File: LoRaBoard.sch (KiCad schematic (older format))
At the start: 22 parts, among them J1 Prog, J2 I2C, J3 UART, J4 GPIO, J5 ADC/SPI, J6 CONN_01X02, J7 PWR, SW1 SWITCH_PUSHBUTTONC&K_KSS, U1 im880b, U2 LDO-TPS78233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

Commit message: Done, panelize
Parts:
- added J8: CONN_01X01, Pin_Headers:Pin_Header_Straight_1x01_Pitch2.54mm, symbol CONN_01X01
- gave numbers to parts that had none: 2
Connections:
- net +3V3: now also J8.1 (P1)
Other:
- moved on the sheet: J7
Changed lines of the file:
@@
 L CONN_01X02 J7
 U 1 1 58D21A9B
-P 9500 750
-F 0 "J7" H 9500 900 50  0000 C CNN
-F 1 "PWR" V 9600 750 50  0000 C CNN
-F 2 "Pin_Headers:Pin_Header_Straight_1x02_Pitch2.54mm" H 9500 750 50  0001 C CNN
-F 3 "" H 9500 750 50  0001 C CNN
-	1    9500 750
+P 9300 750
+F 0 "J7" H 9300 900 50  0000 C CNN
+F 1 "PWR" V 9400 750 50  0000 C CNN
+F 2 "Pin_Headers:Pin_Header_Straight_1x02_Pitch2.54mm" H 9300 750 50  0001 C CNN
+F 3 "" H 9300 750 50  0001 C CNN
+	1    9300 750
 	0    -1   -1   0
 $EndComp
@@
 L GND #PWR01
 U 1 1 58D237F2
-P 9600 950
-F 0 "#PWR01" H 9600 700 50  0001 C CNN
-F 1 "GND" H 9600 800 50  0000 C CNN
-F 2 "" H 9600 950 50  0001 C CNN
-F 3 "" H 9600 950 50  0001 C CNN
-	1    9600 950
+P 9400 950
+F 0 "#PWR01" H 9400 700 50  0001 C CNN
+F 1 "GND" H 9400 800 50  0000 C CNN
+F 2 "" H 9400 950 50  0001 C CNN
+F 3 "" H 9400 950 50  0001 C CNN
+	1    9400 950
 	1    0    0    -1
 $EndComp
@@
 L +BATT #PWR014
 U 1 1 58D245EB
-P 9400 950
-F 0 "#PWR014" H 9400 800 50  0001 C CNN
-F 1 "+BATT" H 9400 1090 50  0000 C CNN
-F 2 "" H 9400 950 50  0001 C CNN
-F 3 "" H 9400 950 50  0001 C CNN
-	1    9400 950
+P 9200 950
+F 0 "#PWR014" H 9200 800 50  0001 C CNN
+F 1 "+BATT" H 9200 1090 50  0000 C CNN
+F 2 "" H 9200 950 50  0001 C CNN
+F 3 "" H 9200 950 50  0001 C CNN
+	1    9200 950
 	-1   0    0    1
 $EndComp
@@
 $EndComp
 Wire Wire Line
-	9450 950  9400 950
-Wire Wire Line
-	9550 950  9600 950
+	9250 950  9200 950
+Wire Wire Line
+	9350 950  9400 950
 Wire Wire Line
 	9350 1600 9350 1650
@@
 	10350 6000 10350 6100
 $Comp
-L RESISTOR0603-RES R?
+L RESISTOR0603-RES R5
 U 1 1 58E2215E
 P 10750 900
-F 0 "R?" H 10600 959 50  0000 L BNN
+F 0 "R5" H 10600 959 50  0000 L BNN
 F 1 "10k" H 10600 770 50  0000 L BNN
 F 2 "Resistors_SMD:R_0603" H 10780 1050 20  0001 C CNN
@@
 $EndComp
 $Comp
-L RESISTOR0603-RES R?
+L RESISTOR0603-RES R4
 U 1 1 58E22264
 P 10450 650
-F 0 "R?" H 10300 709 50  0000 L BNN
+F 0 "R4" H 10300 709 50  0000 L BNN
 F 1 "33k" H 10300 520 50  0000 L BNN
 F 2 "Resistors_SMD:R_0603" H 10480 800 20  0001 C CNN
@@
 	10750 1100 10750 1150
 $Comp
-L GND #PWR?
+L GND #PWR032
 U 1 1 58E22571
 P 10750 1150
-F 0 "#PWR?" H 10750 900 50  0001 C CNN
+F 0 "#PWR032" H 10750 900 50  0001 C CNN
 F 1 "GND" H 10750 1000 50  0000 C CNN
 F 2 "" H 10750 1150 50  0001 C CNN
@@
 $EndComp
 $Comp
-L +BATT #PWR?
+L +BATT #PWR033
 U 1 1 58E225BE
 P 10200 650
-F 0 "#PWR?" H 10200 500 50  0001 C CNN
+F 0 "#PWR033" H 10200 500 50  0001 C CNN
 F 1 "+BATT" H 10200 790 50  0000 C CNN
 F 2 "" H 10200 650 50  0001 C CNN
@@
 Text Label 10900 650  0    60   ~ 0
 P17
+$Comp
+L +3.3V #PWR034
+U 1 1 58E338CA
+P 8650 950
+F 0 "#PWR034" H 8650 800 50  0001 C CNN
+F 1 "+3.3V" H 8650 1090 50  0000 C CNN
+F 2 "" H 8650 950 50  0001 C CNN
+F 3 "" H 8650 950 50  0001 C CNN
+	1    8650 950
+	-1   0    0    1
+$EndComp
+Wire Wire Line
+	8650 850  8650 950
+$Comp
+L CONN_01X01 J8
+U 1 1 58E343EA
+P 8650 650
+F 0 "J8" H 8650 750 50  0000 C CNN
+F 1 "CONN_01X01" V 8750 650 50  0000 C CNN
+F 2 "Pin_Headers:Pin_Header_Straight_1x01_Pitch2.54mm" H 8650 650 50  0001 C CNN
+F 3 "" H 8650 650 50  0001 C CNN
+	1    8650 650
+	0    -1   -1   0
+$EndComp
 $EndSCHEMATC

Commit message: Done
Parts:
- C2, C3: value 0.1u -> 1u
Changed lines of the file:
@@
 P 9950 5000
 F 0 "C3" H 9975 5100 50  0000 L CNN
-F 1 "0.1u" H 9975 4900 50  0000 L CNN
+F 1 "1u" H 9975 4900 50  0000 L CNN
 F 2 "Capacitors_SMD:C_0603" H 9988 4850 50  0001 C CNN
 F 3 "" H 9950 5000 50  0001 C CNN
@@
 P 9100 4600
 F 0 "C2" H 9125 4700 50  0000 L CNN
-F 1 "0.1u" H 8900 4700 50  0000 L CNN
+F 1 "1u" H 8900 4700 50  0000 L CNN
 F 2 "Capacitors_SMD:C_0603" H 9138 4450 50  0001 C CNN
 F 3 "" H 9100 4600 50  0001 C CNN

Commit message: PCB complete, panel complete
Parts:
- removed J1: Prog, Pin_Headers:Pin_Header_Straight_1x03_Pitch2.54mm, symbol CONN_01X03
- removed J2: I2C, Pin_Headers:Pin_Header_Straight_1x03_Pitch2.54mm, symbol CONN_01X03
- removed J3: UART, Pin_Headers:Pin_Header_Straight_1x03_Pitch2.54mm, symbol CONN_01X03
- removed J4: GPIO, Pin_Headers:Pin_Header_Straight_1x04_Pitch2.54mm, symbol CONN_01X04
- removed J5: ADC/SPI, Pin_Headers:Pin_Header_Straight_1x08_Pitch2.54mm, symbol CONN_01X08
- removed J6: CONN_01X02, Pin_Headers:Pin_Header_Straight_1x02_Pitch2.54mm, symbol CONN_01X02
- removed J8: CONN_01X01, Pin_Headers:Pin_Header_Straight_1x01_Pitch2.54mm, symbol CONN_01X01
- removed S1: SWITCH-SPDTPTH2, SparkFun-Electromechanical:SWITCH-SPDT-SMD, symbol SWITCH-SPDTPTH2
- removed SW1: SWITCH_PUSHBUTTONC&K_KSS, BTN_CK_KSS, symbol SWITCH_PUSHBUTTONC&K_KSS
- removed X1: SMACONNECTOR, adafruit:SMA90_DIP, symbol SMACONNECTOR
- added J1: CONN_01X12, Pin_Headers:Pin_Header_Straight_1x12_Pitch2.54mm, symbol CONN_01X12
- added J2: CONN_01X08, Pin_Headers:Pin_Header_Straight_1x08_Pitch2.54mm, symbol CONN_01X08
- added J3: CONN_01X09, Pin_Headers:Pin_Header_Straight_1x09_Pitch2.54mm, symbol CONN_01X09
- added J4: CONN_COAXIAL, Connectors:SMA_THT_Jack_Straight, symbol CONN_COAXIAL
- added J5: SwitchSPST, Buttons_Switches_SMD:SW_SPST_EVQPE1, symbol CONN_01X02
- added J6: CONN_01X01, Pin_Headers:Pin_Header_Straight_1x01_Pitch2.54mm, symbol CONN_01X01
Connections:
- net +3V3: now also J2.5 (P5), J5.1 (P1), J6.1 (P1)
- net +BATT: now also R1.2; no longer R1.1
- net GND: now also J1.11 (P11), J1.6 (P6), J2.4 (P4), J3.2 (P2), J3.7 (P7), J4.2 (Ext); no longer U1.1 (GND)
- net RF: now also J4.1 (In)
- net 4: now reaches U1.4 (P3/JTDO)
- net 4: now also J1.4 (P4)
- net 5: now reaches U1.5 (P4/JTDI)
- net 5: now also J1.5 (P5)
- net BOOT renamed 26
- net 26: now also J3.6 (P6)
- net EN: no longer names the net of U2.3 (EN)
- net EN: now also R1.1
- net JTCK renamed 2
- net 2: now also J1.2 (P2)
- net JTMS renamed 3
- net 3: now also J1.3 (P3)
- net P10 renamed 15
- net 15: now also J2.3 (P3)
- net P11 renamed 20
- net 20: now also J2.8 (P8)
- net P12 renamed 21
- net 21: now also J3.1 (P1)
- net P13 renamed 23
- net 23: now also J3.3 (P3)
- net P14 renamed 24
- net 24: now also J3.4 (P4)
- net P15 renamed 25
- net 25: now also J3.5 (P5)
- net P17 renamed 29
- net 29: now also J3.9 (P9)
- net P5 renamed 8
- net 8: now also J1.8 (P8)
- net P6 renamed 9
- net 9: now also J1.9 (P9)
- net P7 renamed 12
- net 12: now also J1.12 (P12)
- net P8 renamed 13
- net 13: now also J2.1 (P1)
- net P9 renamed 14
- net 14: now also J2.2 (P2)
- net RESET renamed 7
- net 7: now also J1.7 (P7), J5.2 (P2)
- net RXD renamed 18
- net 18: now also J2.6 (P6)
- net TXD renamed 19
- net 19: now also J2.7 (P7)
- new net 1: J1.1 (P1), U1.1 (GND)
- new net 10: J1.10 (P10)
- new net 28: J3.8 (P8)
- no-connect marks 2 -> 0
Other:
- note removed: "P1 - SWCLK - PA_14\nP2 - SWDIO - PA_13\n\n"
- note removed: "P12 - I2C1_SCL - PB_8\nP13 - I2C1_SDA - PB_9\n"
- note removed: "P5 - DIO/UART1_CTS - PA_11\nP6 - DIO/UART1_RTS - PA_12\nP11- DIO - PA_8\n"
- note removed: "P7 - ADC_IN20/SPI2_MISO - PB_14 \nP8 - ADC_IN21/SPI2_MOSI - PB_15\nP9 - ADC_IN19/SPI2_CLK - PB_13\nP10 - ADC_IN18/SPI2_NSS - PB_12\nP14 - ADC_IN1 - PA_1 \nP15 - ADC_IN0 - PA_0\nP17 - ADC_IN3 - PA_3\n"
- note removed: "TXD - USART1_TXD - PA_9\nRXD - USART1_RXD - PA_10/PB_6"

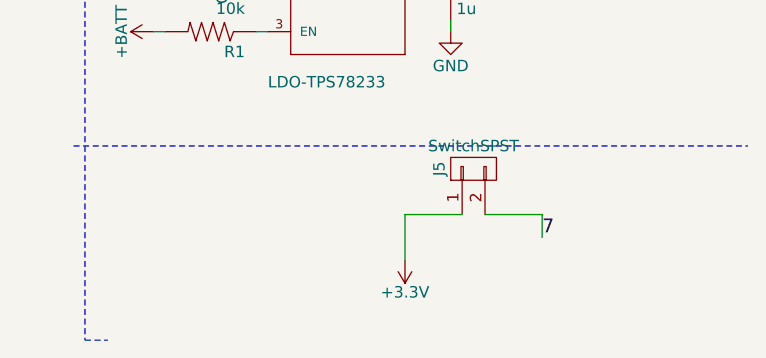
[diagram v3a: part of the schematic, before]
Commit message: Panelization done, send for Fab
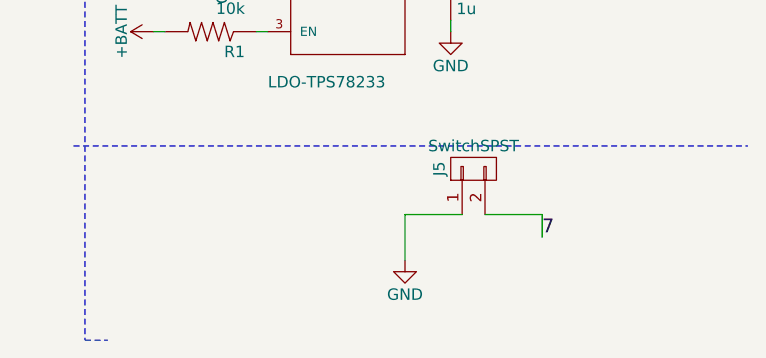
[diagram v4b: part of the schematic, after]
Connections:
- net +3V3: no longer J5.1 (P1)
- net GND: now also J5.1 (P1)
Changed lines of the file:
@@
 LIBS:valves
 LIBS:im880b
+LIBS:GeekAmmo
+LIBS:LilyPad-Wearables
+LIBS:SparkFun-Aesthetics
+LIBS:SparkFun-AnalogIC
+LIBS:SparkFun-Boards
+LIBS:SparkFun-Capacitors
+LIBS:SparkFun-Connectors
+LIBS:SparkFun-DigitalIC
+LIBS:SparkFun-DiscreteSemi
+LIBS:SparkFun-Displays
+LIBS:SparkFun-Electromechanical
+LIBS:SparkFun-FreqCtrl
+LIBS:SparkFun-LED
+LIBS:SparkFun-Passives
+LIBS:SparkFun-PowerIC
+LIBS:SparkFun-RF
+LIBS:SparkFun-Resistors
+LIBS:SparkFun-Retired
+LIBS:SparkFun-Sensors
+LIBS:Teensy_3_and_LC_Series_Boards_v1.1
+LIBS:User-Submitted
+LIBS:adafruit
 LIBS:LoRaBoard-cache
-EELAYER 26 0
+EELAYER 25 0
 EELAYER END
 $Descr A4 11693 8268
@@
 F 3 "" H 9100 4400 50  0001 C CNN
 	1    9100 4400
-	-1   0    0    1
-$EndComp
-$Comp
-L +3.3V #PWR011
-U 1 1 58D26862
-P 9750 6200
-F 0 "#PWR011" H 9750 6050 50  0001 C CNN
-F 1 "+3.3V" H 9750 6340 50  0000 C CNN
-F 2 "" H 9750 6200 50  0001 C CNN
-F 3 "" H 9750 6200 50  0001 C CNN
-	1    9750 6200
 	-1   0    0    1
 $EndComp
@@
 	-1   0    0    1
 $EndComp
+$Comp
+L GND #PWR?
+U 1 1 58EB76AE
+P 9750 6200
+F 0 "#PWR?" H 9750 5950 50  0001 C CNN
+F 1 "GND" H 9750 6050 50  0000 C CNN
+F 2 "" H 9750 6200 50  0001 C CNN
+F 3 "" H 9750 6200 50  0001 C CNN
+	1    9750 6200
+	1    0    0    -1
+$EndComp
 $EndSCHEMATC
